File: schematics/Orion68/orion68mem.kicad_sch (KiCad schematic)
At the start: 0 parts

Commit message: Schematics update
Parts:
- added J5: Euro96pin, ConnPdSilva:conn_euro96, symbol ConnPdSilva:ConnEuro96
- added U100: GAL16V8, symbol Logic_Programmable:GAL16V8
- added U101, U103, U105, U107: RAM_LOW, Package_DIP:DIP-32_W15.24mm, symbol Memory_RAM:AS6C4008-55PCN
- added U102, U104, U106, U108: RAM_HIGH, Package_DIP:DIP-32_W15.24mm, symbol Memory_RAM:AS6C4008-55PCN
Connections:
- new net +12V: J5.92
- new net +5V: J5.1, J5.33, J5.65, U100.20 (VCC), U101.32 (VCC), U102.32 (VCC), U103.32 (VCC), U104.32 (VCC), U105.32 (VCC), U106.32 (VCC), U107.32 (VCC), U108.32 (VCC)
- new net -5V: J5.94
- new net ALE: J5.73
- new net BA0: J5.18
- new net BA1: J5.19, U101.12 (A0), U102.12 (A0), U103.12 (A0), U104.12 (A0), U105.12 (A0), U106.12 (A0), U107.12 (A0), U108.12 (A0)
- new net BA10: J5.28, U101.26 (A9), U102.26 (A9), U103.26 (A9), U104.26 (A9), U105.26 (A9), U106.26 (A9), U107.26 (A9), U108.26 (A9)
- new net BA11: J5.29, U101.23 (A10), U102.23 (A10), U103.23 (A10), U104.23 (A10), U105.23 (A10), U106.23 (A10), U107.23 (A10), U108.23 (A10)
- new net BA12: J5.30, U101.25 (A11), U102.25 (A11), U103.25 (A11), U104.25 (A11), U105.25 (A11), U106.25 (A11), U107.25 (A11), U108.25 (A11)
- new net BA13: J5.31, U101.4 (A12), U102.4 (A12), U103.4 (A12), U104.4 (A12), U105.4 (A12), U106.4 (A12), U107.4 (A12), U108.4 (A12)
- new net BA14: J5.63, U101.28 (A13), U102.28 (A13), U103.28 (A13), U104.28 (A13), U105.28 (A13), U106.28 (A13), U107.28 (A13), U108.28 (A13)
- new net BA15: J5.62, U101.3 (A14), U102.3 (A14), U103.3 (A14), U104.3 (A14), U105.3 (A14), U106.3 (A14), U107.3 (A14), U108.3 (A14)
- new net BA16: J5.61, U101.31 (A15), U102.31 (A15), U103.31 (A15), U104.31 (A15), U105.31 (A15), U106.31 (A15), U107.31 (A15), U108.31 (A15)
- new net BA17: J5.60, U101.2 (A16), U102.2 (A16), U103.2 (A16), U104.2 (A16), U105.2 (A16), U106.2 (A16), U107.2 (A16), U108.2 (A16)
- new net BA18: J5.59, U101.30 (A17), U102.30 (A17), U103.30 (A17), U104.30 (A17), U105.30 (A17), U106.30 (A17), U107.30 (A17), U108.30 (A17)
- new net BA19: J5.58, U101.1 (A18), U102.1 (A18), U103.1 (A18), U104.1 (A18), U105.1 (A18), U106.1 (A18), U107.1 (A18), U108.1 (A18)
- new net BA2: J5.20, U101.11 (A1), U102.11 (A1), U103.11 (A1), U104.11 (A1), U105.11 (A1), U106.11 (A1), U107.11 (A1), U108.11 (A1)
- new net BA20: J5.57, U100.1 (I1/CLK)
- new net BA21: J5.56, U100.2 (I2)
- new net BA22: J5.55, U100.3 (I3)
- new net BA23: J5.54, U100.4 (I4)
- new net BA3: J5.21, U101.10 (A2), U102.10 (A2), U103.10 (A2), U104.10 (A2), U105.10 (A2), U106.10 (A2), U107.10 (A2), U108.10 (A2)
- new net BA4: J5.22, U101.9 (A3), U102.9 (A3), U103.9 (A3), U104.9 (A3), U105.9 (A3), U106.9 (A3), U107.9 (A3), U108.9 (A3)
- new net BA5: J5.23, U101.8 (A4), U102.8 (A4), U103.8 (A4), U104.8 (A4), U105.8 (A4), U106.8 (A4), U107.8 (A4), U108.8 (A4)
- new net BA6: J5.24, U101.7 (A5), U102.7 (A5), U103.7 (A5), U104.7 (A5), U105.7 (A5), U106.7 (A5), U107.7 (A5), U108.7 (A5)
- new net BA7: J5.25, U101.6 (A6), U102.6 (A6), U103.6 (A6), U104.6 (A6), U105.6 (A6), U106.6 (A6), U107.6 (A6), U108.6 (A6)
- new net BA8: J5.26, U101.5 (A7), U102.5 (A7), U103.5 (A7), U104.5 (A7), U105.5 (A7), U106.5 (A7), U107.5 (A7), U108.5 (A7)
- new net BA9: J5.27, U101.27 (A8), U102.27 (A8), U103.27 (A8), U104.27 (A8), U105.27 (A8), U106.27 (A8), U107.27 (A8), U108.27 (A8)
- new net BD0: J5.2, U101.13 (DQ0), U103.13 (DQ0), U105.13 (DQ0), U107.13 (DQ0)
- new net BD1: J5.3, U101.14 (DQ1), U103.14 (DQ1), U105.14 (DQ1), U107.14 (DQ1)
- new net BD10: J5.12, U102.15 (DQ2), U104.15 (DQ2), U106.15 (DQ2), U108.15 (DQ2)
- new net BD11: J5.13, U102.17 (DQ3), U104.17 (DQ3), U106.17 (DQ3), U108.17 (DQ3)
- new net BD12: J5.14, U102.18 (DQ4), U104.18 (DQ4), U106.18 (DQ4), U108.18 (DQ4)
- new net BD13: J5.15, U102.19 (DQ5), U104.19 (DQ5), U106.19 (DQ5), U108.19 (DQ5)
- new net BD14: J5.16, U102.20 (DQ6), U104.20 (DQ6), U106.20 (DQ6), U108.20 (DQ6)
- new net BD15: J5.17, U102.21 (DQ7), U104.21 (DQ7), U106.21 (DQ7), U108.21 (DQ7)
- new net BD2: J5.4, U101.15 (DQ2), U103.15 (DQ2), U105.15 (DQ2), U107.15 (DQ2)
- new net BD3: J5.5, U101.17 (DQ3), U103.17 (DQ3), U105.17 (DQ3), U107.17 (DQ3)
- new net BD4: J5.6, U101.18 (DQ4), U103.18 (DQ4), U105.18 (DQ4), U107.18 (DQ4)
- new net BD5: J5.7, U101.19 (DQ5), U103.19 (DQ5), U105.19 (DQ5), U107.19 (DQ5)
- new net BD6: J5.8, U101.20 (DQ6), U103.20 (DQ6), U105.20 (DQ6), U107.20 (DQ6)
- new net BD7: J5.9, U101.21 (DQ7), U103.21 (DQ7), U105.21 (DQ7), U107.21 (DQ7)
- new net BD8: J5.10, U102.13 (DQ0), U104.13 (DQ0), U106.13 (DQ0), U108.13 (DQ0)
- new net BD9: J5.11, U102.14 (DQ1), U104.14 (DQ1), U106.14 (DQ1), U108.14 (DQ1)
- new net BOOTIN: J5.87, U100.8 (I8)
- new net B/cpurd: J5.45, U100.9 (I9), U101.24 (OE#), U102.24 (OE#), U103.24 (OE#), U104.24 (OE#), U105.24 (OE#), U106.24 (OE#), U107.24 (OE#), U108.24 (OE#)
- new net B/cpurw: J5.46, U100.11 (I10/~{OE}), U101.29 (WE#), U102.29 (WE#), U103.29 (WE#), U104.29 (WE#), U105.29 (WE#), U106.29 (WE#), U107.29 (WE#), U108.29 (WE#)
- new net CPU_CLK: J5.81
- new net CRUCLK: J5.35
- new net CRUIN: J5.36
- new net CRUOUT: J5.37
- new net DBIN: J5.38
- new net DT/R: J5.75
- new net E: J5.34
- new net GND: J5.32, J5.64, J5.93, J5.95, J5.96, U100.10 (GND), U101.16 (VSS), U102.16 (VSS), U103.16 (VSS), U104.16 (VSS), U105.16 (VSS), U106.16 (VSS), U107.16 (VSS), U108.16 (VSS)
- new net HLDA: J5.52
- new net IAQ: J5.39
- new net IC3: J5.47
- new net IRQ2: J5.48
- new net IRQ3: J5.49
- new net IRQ4: J5.50
- new net IRQ5: J5.89
- new net IRQ6: J5.90
- new net IRQ7: J5.91
- new net M/IO: J5.76
- new net NMI: J5.41
- new net PWR_GOOD: J5.88
- new net RDY: J5.44
- new net RESET: J5.67
- new net Res9: J5.69
- new net TICK_IN: J5.86
- new net /AS: J5.43
- new net /BAS: U100.5 (I5)
- new net /BERR: J5.68
- new net /BLDS: U100.6 (I6)
- new net /BUDS: U100.7 (I7)
- new net /DEN: J5.74
- new net /HALT: J5.53
- new net /HOLD: J5.42
- new net /INTA: J5.72
- new net /INTR: J5.40
- new net /IO_CS: J5.85
- new net /LDS: J5.70
- new net /M1: J5.79
- new net /RAM1CS_H: U100.18 (IO2), U102.22 (CE#)
- new net /RAM1CS_L: U100.19 (IO1), U101.22 (CE#)
- new net /RAM2CS_H: U100.16 (IO4), U104.22 (CE#)
- new net /RAM2CS_L: U100.17 (I03), U103.22 (CE#)
- new net /RAM3CS_H: U100.14 (IO6), U106.22 (CE#)
- new net /RAM3CS_L: U100.15 (IO5), U105.22 (CE#)
- new net /RAM4CS_H: U100.12 (IO8), U108.22 (CE#)
- new net /RAM4CS_L: U100.13 (IO7), U107.22 (CE#)
- new net /RESET: J5.66
- new net /RFSH: J5.80
- new net /RST: J5.51
- new net /SSO: J5.77
- new net /UDS: J5.71
- new net /WAIT: J5.78

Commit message: Schematics update
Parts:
- U100: footprint (none) -> Package_DIP:DIP-20_W7.62mm
- renumbered J5 to J100
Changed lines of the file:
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@@
 		(on_board yes)
 		(dnp no)
-		(property "Reference" "J5"
+		(property "Reference" "J100"
 			(at 246.634 24.892 0)
 			(effects
@@
 			(project "Orion68"
 				(path "/c7ab032b-c937-44de-ab42-c91dee57f0a8/70b7defe-43f8-4fe6-9382-ae901438ae75"
-					(reference "J5")
+					(reference "J100")
 					(unit 1)
 				)
@@
 			)
 		)
-		(property "Footprint" ""
+		(property "Footprint" "Package_DIP:DIP-20_W7.62mm"
 			(at 39.37 181.61 0)
 			(effects

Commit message: Schematic update
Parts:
- removed J100: Euro96pin, ConnPdSilva:conn_euro96, symbol ConnPdSilva:ConnEuro96
- added J4: Euro96pin, ConnPdSilva:conn_euro96, symbol ConnPdSilva:ConnEuro96
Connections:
- net +12V: now also J4.92
- net +5V: now also J4.1, J4.33, J4.65
- net -5V: now also J4.94
- net ALE: now also J4.73
- net BA0: now also J4.18
- net BA1: now also J4.19
- net BA10: now also J4.28
- net BA11: now also J4.29
- net BA12: now also J4.30
- net BA13: now also J4.31
- net BA14: now also J4.63
- net BA15: now also J4.62
- net BA16: now also J4.61
- net BA17: now also J4.60
- net BA18: now also J4.59
- net BA19: now also J4.58
- net BA2: now also J4.20
- net BA20: now also J4.57
- net BA21: now also J4.56
- net BA22: now also J4.55
- net BA23: now also J4.54
- net BA3: now also J4.21
- net BA4: now also J4.22
- net BA5: now also J4.23
- net BA6: now also J4.24
- net BA7: now also J4.25
- net BA8: now also J4.26
- net BA9: now also J4.27
- net BD0: now also J4.2
- net BD1: now also J4.3
- net BD10: now also J4.12
- net BD11: now also J4.13
- net BD12: now also J4.14
- net BD13: now also J4.15
- net BD14: now also J4.16
- net BD15: now also J4.17
- net BD2: now also J4.4
- net BD3: now also J4.5
- net BD4: now also J4.6
- net BD5: now also J4.7
- net BD6: now also J4.8
- net BD7: now also J4.9
- net BD8: now also J4.10
- net BD9: now also J4.11
- net BOOTIN: now also J4.87
- net B/cpurd: now also J4.45; no longer U100.9 (I9)
- net B/cpurw: no longer U100.11 (I10/~{OE})
- net CPU_CLK: now also J4.81
- net CRUCLK: now also J4.35
- net CRUIN: now also J4.36
- net CRUOUT: now also J4.37
- net DBIN: now also J4.38
- net DT/R: now also J4.75
- net E: now also J4.34
- net GND: now also J4.32, J4.64, J4.93, J4.95, J4.96
- net HLDA: now also J4.52
- net IAQ: now also J4.39
- net IC3: now also J4.47
- net IRQ2: now also J4.48
- net IRQ3: now also J4.49
- net IRQ4: now also J4.50
- net IRQ5: now also J4.89
- net IRQ6: now also J4.90
- net IRQ7: now also J4.91
- net M/IO: now also J4.76
- net NMI: now also J4.41
- net PWR_GOOD: now also J4.88
- net RDY: now also J4.44
- net RESET: now also J4.67
- net Res9: now also J4.69
- net TICK_IN: now also J4.86
- net /BERR: now also J4.68
- net /DEN: now also J4.74
- net /HALT: now also J4.53
- net /HOLD: now also J4.42
- net /INTA: now also J4.72
- net /INTR: now also J4.40
- net /IO_CS: now also J4.85
- net /M1: now also J4.79
- net /RESET: now also J4.66
- net /RFSH: now also J4.80
- net /RST: now also J4.51
- net /SSO: now also J4.77
- net /WAIT: now also J4.78
- net /BAS renamed B/AS
- net B/AS: now also J4.43
- net /BLDS renamed B/LDS
- net B/LDS: now also J4.70
- net /BUDS renamed B/UDS
- net B/UDS: now also J4.71
- new net B/cpuwr: J4.46
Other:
- moved on the sheet: U100, U105, U106, U107, U108

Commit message: Updating
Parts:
- renumbered J4 to J100
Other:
- note added: "Memory board - 100"
- note removed: "Memory board"
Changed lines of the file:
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@@
 		)
 	)
-	(text "Memory board"
+	(text "Memory board  -  100"
 		(exclude_from_sim no)
-		(at 310.896 256.286 0)
+		(at 318.008 255.778 0)
 		(effects
 			(font
 				(size 2 2)
+				(thickness 0.4)
+				(bold yes)
 			)
 		)
@@
 		(on_board yes)
 		(dnp no)
-		(property "Reference" "J4"
+		(property "Reference" "J100"
 			(at 157.734 97.282 0)
 			(effects
@@
 			(project "Orion68"
 				(path "/c7ab032b-c937-44de-ab42-c91dee57f0a8/70b7defe-43f8-4fe6-9382-ae901438ae75"
-					(reference "J4")
+					(reference "J100")
 					(unit 1)
 				)

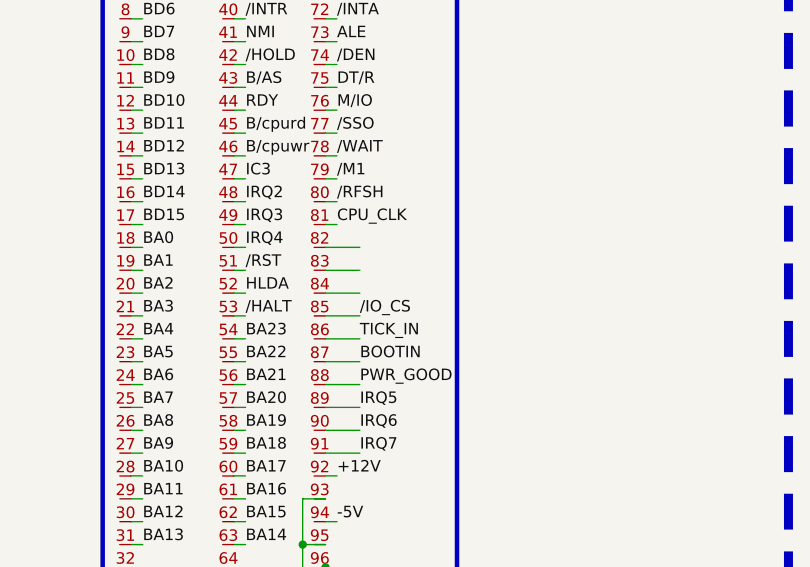
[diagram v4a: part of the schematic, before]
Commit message: Schematic verified to board
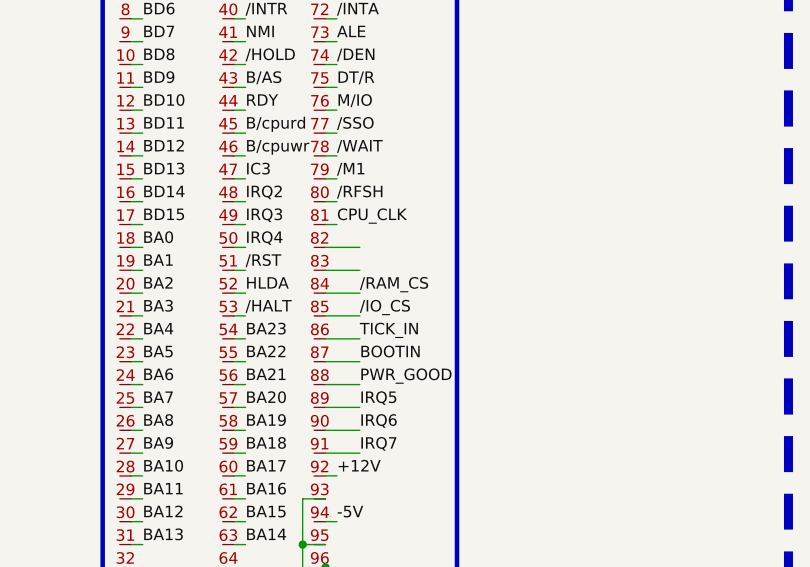
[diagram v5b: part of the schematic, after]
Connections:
- net /RAM_CS: now reaches J100.84
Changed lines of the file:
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@@
 			(font
 				(size 1.27 1.27)
+				(color 0 255 0 1)
 			)
 			(justify left bottom)
@@
 			(font
 				(size 1.27 1.27)
+				(color 0 255 0 1)
 			)
 			(justify left bottom)
@@
 			(font
 				(size 1.27 1.27)
+				(color 0 255 0 1)
 			)
 			(justify left bottom)
@@
 			(font
 				(size 1.27 1.27)
+				(color 0 255 0 1)
 			)
 			(justify left bottom)
@@
 			(font
 				(size 1.27 1.27)
+				(color 0 255 0 1)
 			)
 			(justify left bottom)
@@
 			(font
 				(size 1.27 1.27)
+				(color 0 255 0 1)
 			)
 			(justify left bottom)
@@
 			(font
 				(size 1.27 1.27)
+				(color 0 255 0 1)
 			)
 			(justify left bottom)
@@
 			(font
 				(size 1.27 1.27)
+				(color 0 255 0 1)
 			)
 			(justify left bottom)
@@
 			(font
 				(size 1.27 1.27)
+				(color 0 255 0 1)
 			)
 			(justify left bottom)
@@
 			(font
 				(size 1.27 1.27)
+				(color 0 255 0 1)
 			)
 			(justify left bottom)
@@
 			(font
 				(size 1.27 1.27)
+				(color 0 255 0 1)
 			)
 			(justify left bottom)
@@
 			(font
 				(size 1.27 1.27)
+				(color 0 255 0 1)
 			)
 			(justify left bottom)
@@
 			(font
 				(size 1.27 1.27)
+				(color 0 255 0 1)
 			)
 			(justify left bottom)
@@
 			(font
 				(size 1.27 1.27)
+				(color 0 255 0 1)
 			)
 			(justify left bottom)
@@
 		)
 	)
+	(label "{slash}RAM_CS"
+		(at 172.72 149.86 0)
+		(effects
+			(font
+				(size 1.27 1.27)
+			)
+			(justify left bottom)
+		)
+	)
 	(label "BA4"
 		(at 73.66 34.29 180)
@@
 			(font
 				(size 1.27 1.27)
+				(color 0 255 0 1)
 			)
 			(justify left bottom)
@@
 			(font
 				(size 1.27 1.27)
+				(color 0 255 0 1)
 			)
 			(justify left bottom)
@@
 			(font
 				(size 1.27 1.27)
+				(color 0 255 0 1)
 			)
 			(justify left bottom)
@@
 			(font
 				(size 1.27 1.27)
+				(color 0 255 0 1)
 			)
 			(justify left bottom)
@@
 			(font
 				(size 1.27 1.27)
+				(color 0 255 0 1)
 			)
 			(justify left bottom)
@@
 			(font
 				(size 1.27 1.27)
+				(color 0 255 0 1)
 			)
 			(justify left bottom)
@@
 			(font
 				(size 1.27 1.27)
+				(color 0 255 0 1)
 			)
 			(justify left bottom)
@@
 			(font
 				(size 1.27 1.27)
+				(color 0 255 0 1)
 			)
 			(justify left bottom)
@@
 			(font
 				(size 1.27 1.27)
+				(color 0 255 0 1)
 			)
 			(justify left bottom)
@@
 			(font
 				(size 1.27 1.27)
+				(color 0 255 0 1)
 			)
 			(justify left bottom)

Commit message: Cpu board fixed and running
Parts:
- added U100: GAL20V8, Package_DIP:DIP-24_W7.62mm_Socket, symbol plds:GAL20V8
- added U2.3: 74LS138, symbol 74xx:74LS138
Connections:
- net +5V: now also U100.24 (VCC), U2.3.16 (VCC)
- net BA17: now also U100.8 (I)
- net BA18: now also U100.9 (I)
- net BA19: now also U100.10 (I)
- net BA20: now also U100.1 (I/CLK); no longer U100.1 (I1/CLK)
- net BA21: now also U100.2 (I); no longer U100.2 (I2)
- net BA22: now also U100.3 (I); no longer U100.3 (I3)
- net BA23: now also U100.4 (I); no longer U100.4 (I4)
- net BOOTIN: no longer U100.8 (I8)
- net B/AS: now also U100.5 (I); no longer U100.5 (I5)
- net B/LDS: now also U100.6 (I); no longer U100.6 (I6)
- net B/UDS: now also U100.7 (I); no longer U100.7 (I7)
- net GND: now also U100.12 (GND), U2.3.8 (GND); no longer U100.10 (GND)
- net /RAM1CS_H: now also U100.22 (O); no longer U100.18 (IO2)
- net /RAM1CS_L: now also U100.19 (O); no longer U100.19 (IO1)
- net /RAM2CS_H: now also U100.20 (O); no longer U100.16 (IO4)
- net /RAM2CS_L: now also U100.21 (O); no longer U100.17 (I03)
- net /RAM3CS_H: now also U100.17 (O); no longer U100.14 (IO6)
- net /RAM3CS_L: now also U100.18 (O); no longer U100.15 (IO5)
- net /RAM4CS_H: now also U100.15 (O); no longer U100.12 (IO8)
- net /RAM4CS_L: now also U100.16 (O); no longer U100.13 (IO7)
- net /IO_CS: no longer names the net of J100.85
- net /RAM_CS: no longer names the net of J100.84
- new net A19: U2.3.1 (A0)
- new net A20: U2.3.2 (A1)
- new net A21: U2.3.3 (A2)
- new net A22: U2.3.5 (E2)
- new net A23: U2.3.4 (E1)
- new net ram1_high: U2.3.14 (O1)
- new net ram1_low: U2.3.15 (O0)
- new net ram2_high: U2.3.12 (O3)
- new net ram2_low: U2.3.13 (O2)
- new net ram3_high: U2.3.10 (O5)
- new net ram3_low: U2.3.11 (O4)
- new net ram4_high: U2.3.7 (O7)
- new net ram4_low: U2.3.9 (O6)
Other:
- moved on the sheet: U100

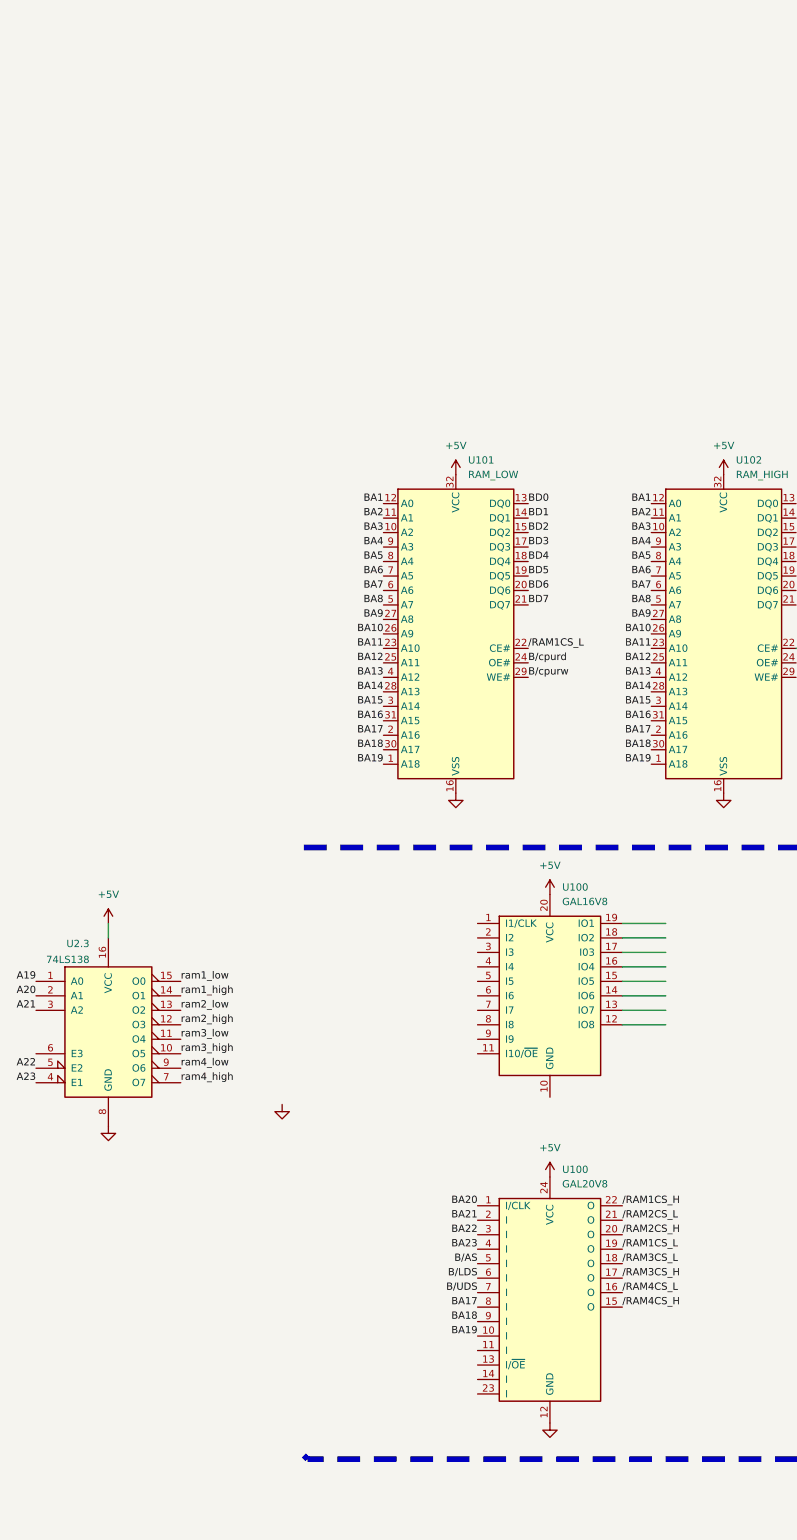
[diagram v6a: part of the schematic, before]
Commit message: New cpu board with NMOS running
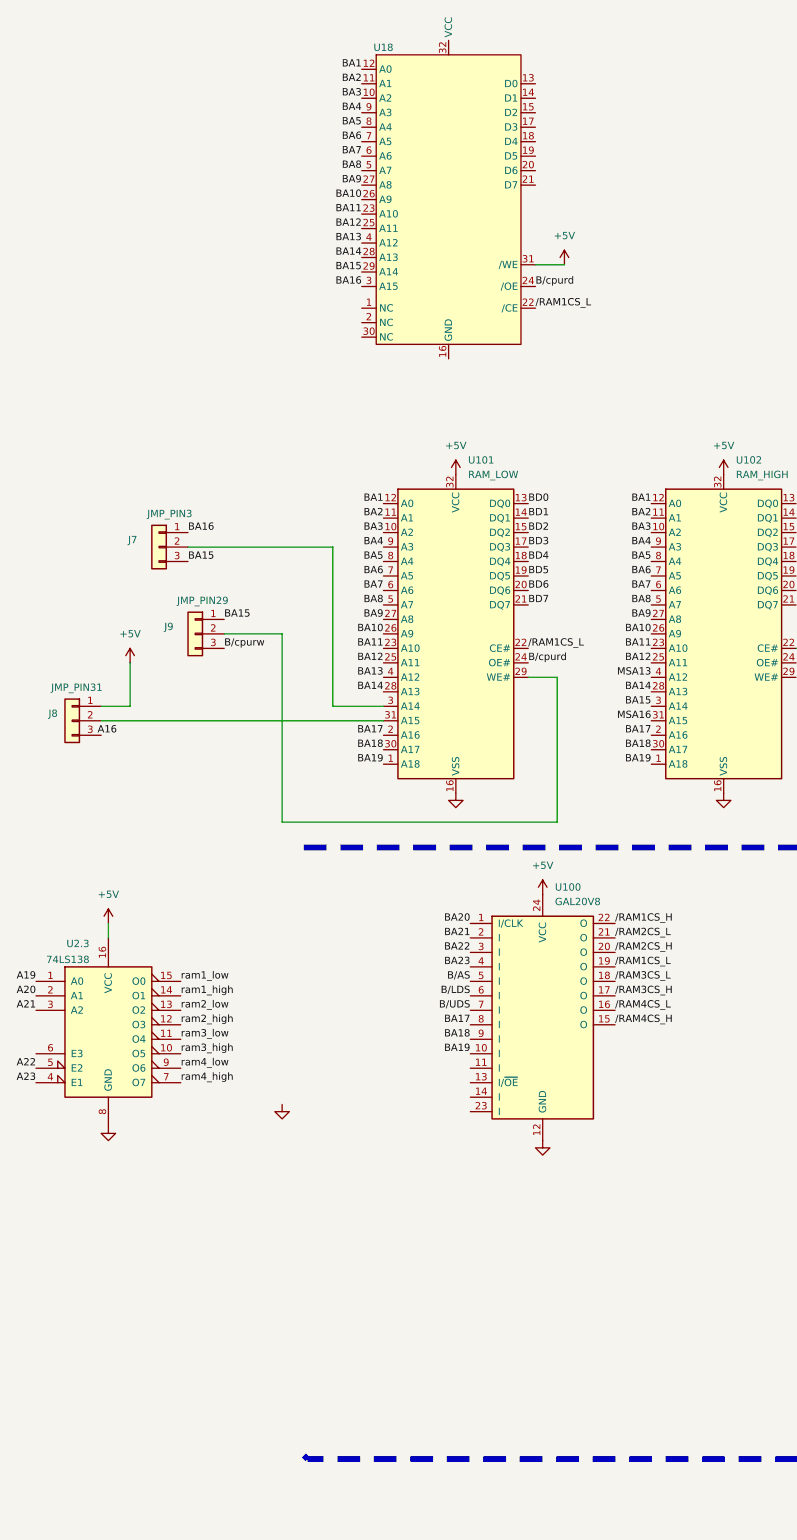
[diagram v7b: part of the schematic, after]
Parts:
- removed U100: GAL16V8, Package_DIP:DIP-20_W7.62mm, symbol Logic_Programmable:GAL16V8
- added J7: JMP_PIN3, symbol Connector_Generic:Conn_01x03
- added J8: JMP_PIN31, symbol Connector_Generic:Conn_01x03
- added J9: JMP_PIN29, symbol Connector_Generic:Conn_01x03
- added U18: ~, symbol pdSilva:AT29C512
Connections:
- net +5V: now also J8.1 (Pin_1), U18.31 (/WE)
- net BA1: now also U18.12 (A0)
- net BA10: now also U18.26 (A9)
- net BA11: now also U18.23 (A10)
- net BA12: now also U18.25 (A11)
- net BA13: now also U18.4 (A12); no longer U102.4 (A12)
- net BA14: now also U18.28 (A13)
- net BA15: now also J7.3 (Pin_3), J9.1 (Pin_1), U18.29 (A14); no longer U101.3 (A14)
- net BA16: now also J7.1 (Pin_1), U18.3 (A15); no longer U101.31 (A15), U102.31 (A15)
- net BA2: now also U18.11 (A1)
- net BA3: now also U18.10 (A2)
- net BA4: now also U18.9 (A3)
- net BA5: now also U18.8 (A4)
- net BA6: now also U18.7 (A5)
- net BA7: now also U18.6 (A6)
- net BA8: now also U18.5 (A7)
- net BA9: now also U18.27 (A8)
- net B/cpurd: now also U18.24 (/OE)
- net B/cpurw: now also J9.3 (Pin_3); no longer U101.29 (WE#)
- net /RAM1CS_L: now also U18.22 (/CE)
- new net: J9.2 (Pin_2), U101.29 (WE#)
- new net: J7.2 (Pin_2), U101.3 (A14)
- new net: J8.2 (Pin_2), U101.31 (A15)
- new net MSA13: U102.4 (A12)
- new net MSA16: U102.31 (A15)
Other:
- moved on the sheet: U100
